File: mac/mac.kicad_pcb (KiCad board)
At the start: 2 copper layers, 5 parts

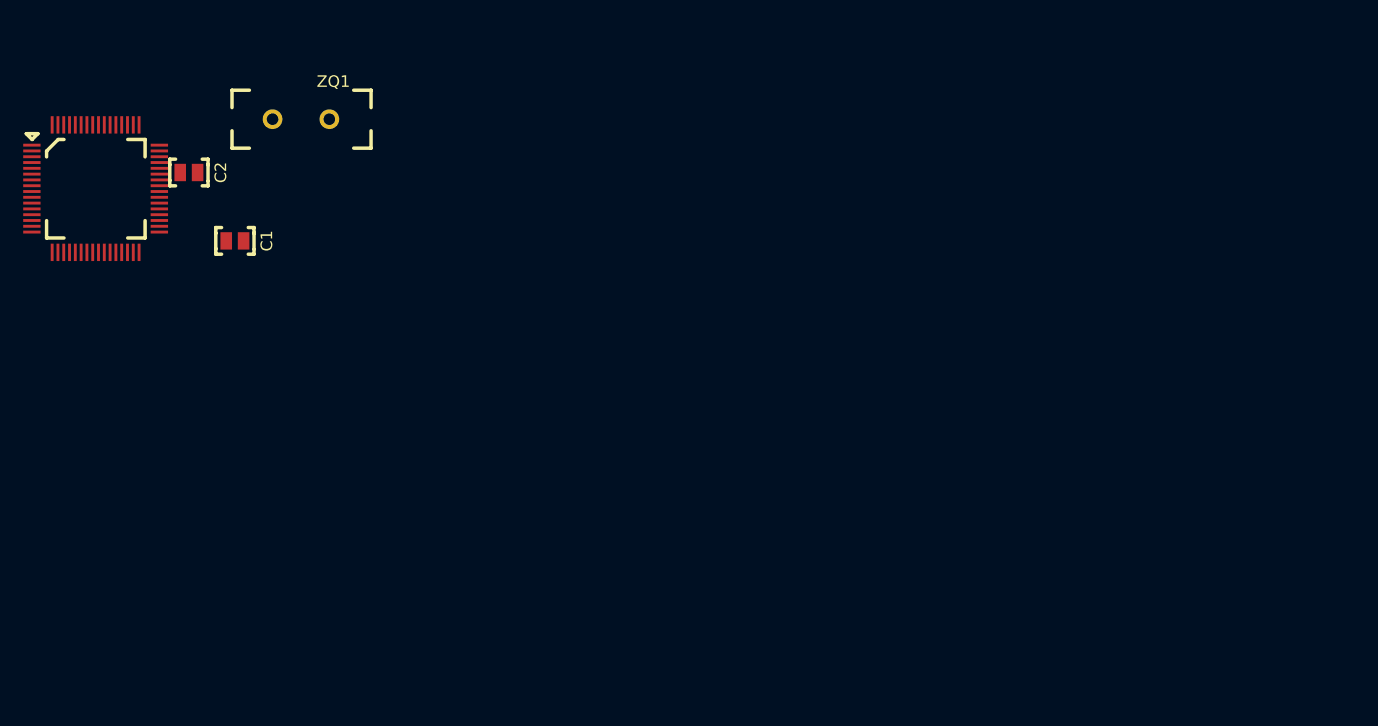
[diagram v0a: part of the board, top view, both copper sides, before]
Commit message: на схеме (-), на трассировке (*)
-поставлен uart-rs485
-поставлена микросхема CAN
-CAN и RS выведены наружу
-выводные разъемы
*определен максимальный габарит 45х70
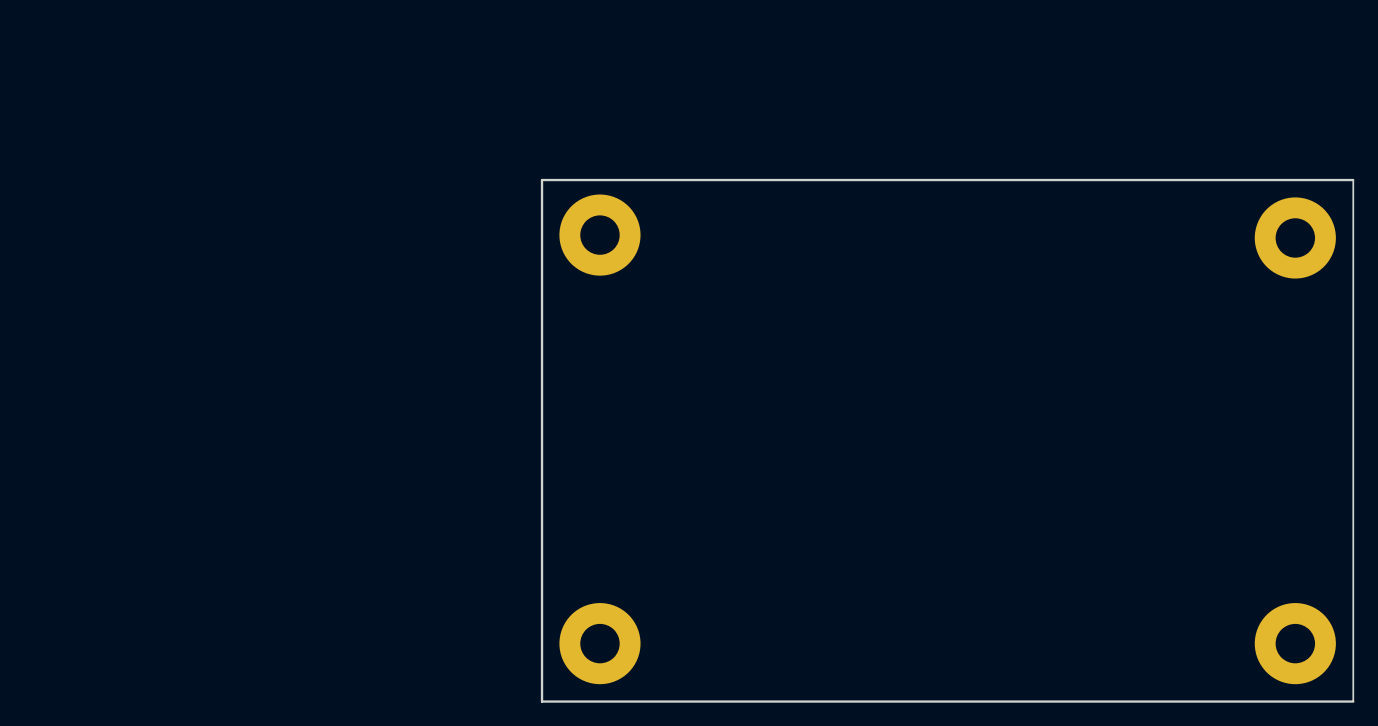
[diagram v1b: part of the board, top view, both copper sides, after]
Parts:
- removed C1, C2: 12пФ, N_RLC:Конденсатор_SMD_0603
- removed DD1: 1986ВЕ92QL, N_DD:Микросхема_1986ВЕ92QL
- removed ZQ1: 16М, N_RLC:Резонатор_РК456МДУ(DIP)
- added M3: Отверстие_М3, N_X:Отверстие_М3, F.Cu at (160.0, 112.5)
- added M3: Отверстие_М3, N_X:Отверстие_М3, F.Cu at (220.0, 112.5)
- added M3: Отверстие_М3, N_X:Отверстие_М3, F.Cu at (220.0, 77.5)
- added M3: Отверстие_М3, N_X:Отверстие_М3, F.Cu at (160.0, 77.2)
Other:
- board outline added: 70 x 45 mm

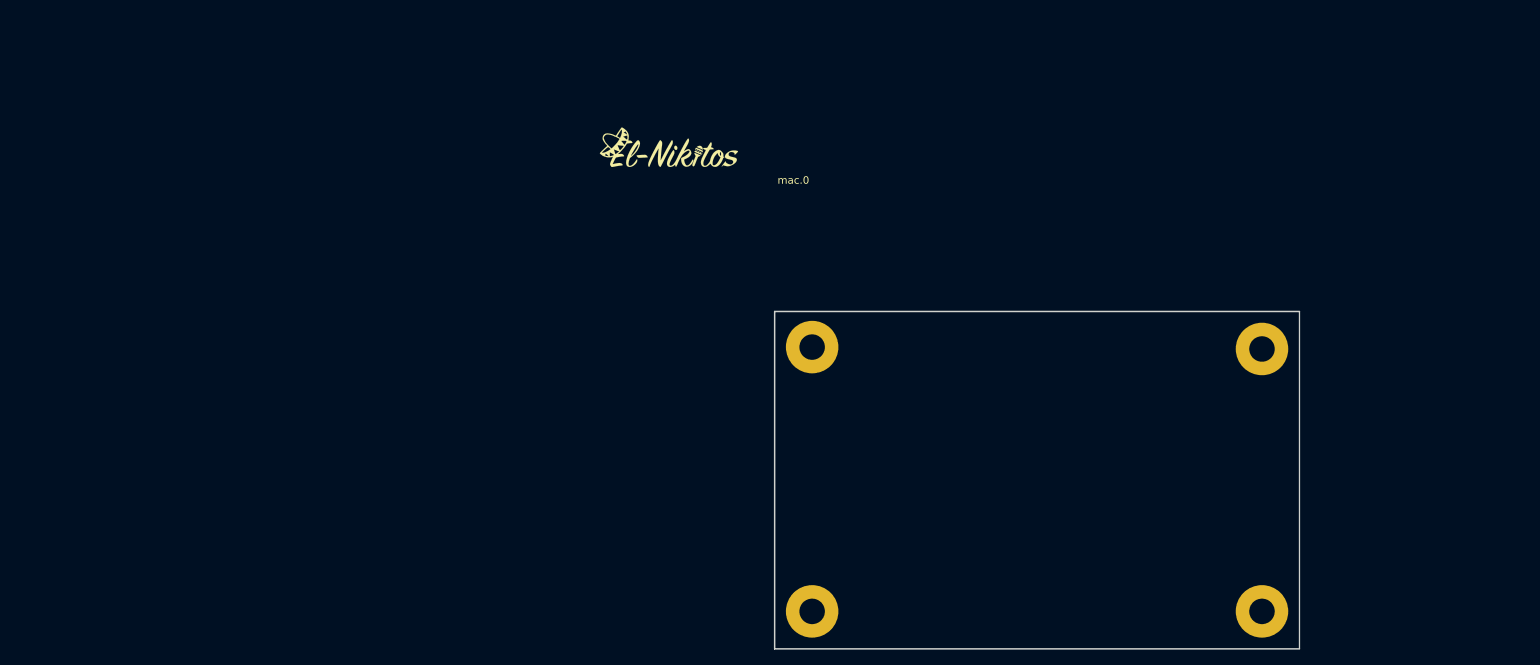
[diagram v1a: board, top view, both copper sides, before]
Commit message: трассировка в самом разгаре
выведены GPIO
не выведены ответвления на RS и CAN
не выведено программирование
не разведена земля
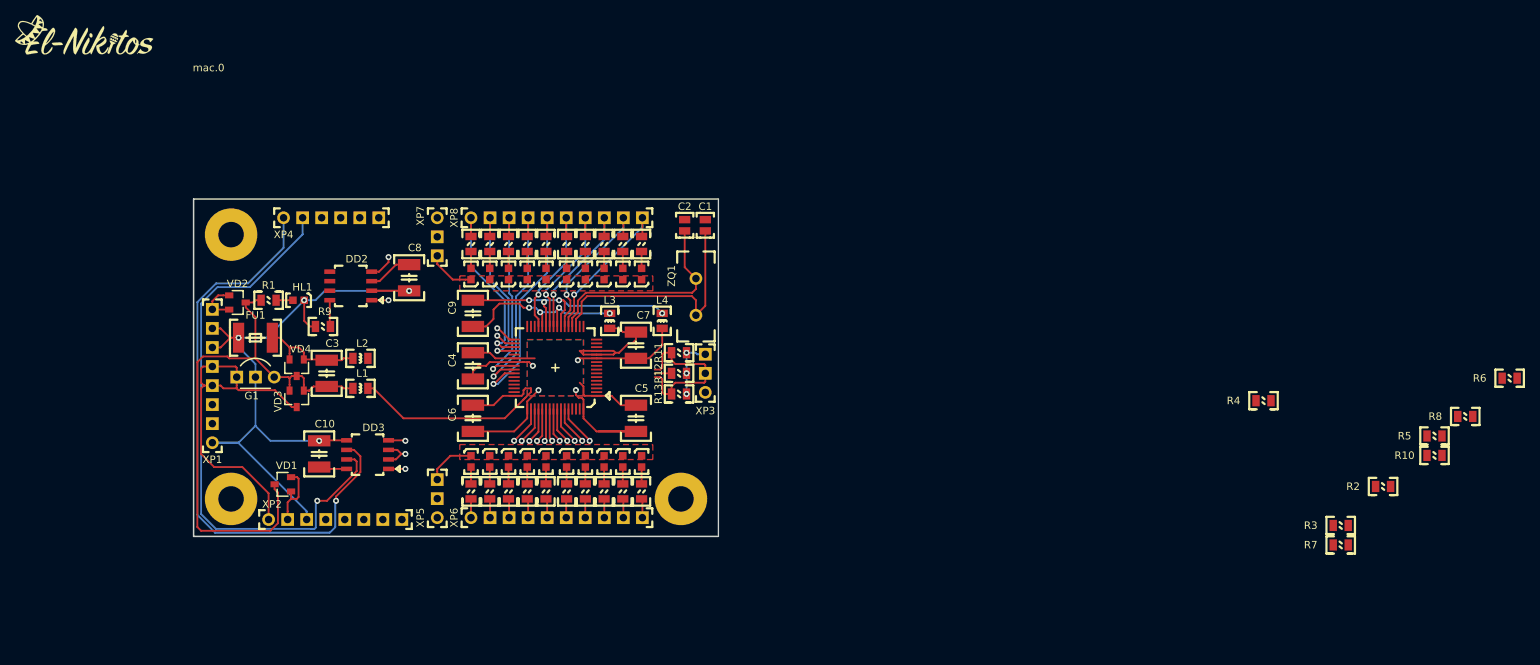
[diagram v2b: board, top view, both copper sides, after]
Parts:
- removed the M3 at (160.0, 112.5)
- removed the M3 at (220.0, 112.5)
- removed the M3 at (220.0, 77.5)
- added C1: 12пФ(0603), N_RLC:Конденсатор_SMD_0603, F.Cu at (145.8, 61.8)
- added C10: 4,7мкФ(1210), N_RLC:Конденсатор_SMD_1210, F.Cu at (94.2, 89.8)
- added C2: 12пФ(0603), N_RLC:Конденсатор_SMD_0603, F.Cu at (143.0, 61.8)
- added C3: 4,7мкФ(1210), N_RLC:Конденсатор_SMD_1210, F.Cu at (95.2, 82.5)
- added C4: 4,7мкФ(1210), N_RLC:Конденсатор_SMD_1210, F.Cu at (114.8, 78.0)
- added C5: 4,7мкФ(1210), N_RLC:Конденсатор_SMD_1210, F.Cu at (136.5, 85.0)
- added C6: 4,7мкФ(1210), N_RLC:Конденсатор_SMD_1210, F.Cu at (114.8, 85.0)
- added C7: 4,7мкФ(1210), N_RLC:Конденсатор_SMD_1210, F.Cu at (136.5, 75.2)
- added C8: 4,7мкФ(1210), N_RLC:Конденсатор_SMD_1210, F.Cu at (106.2, 69.8)
- added C9: 4,7мкФ(1210), N_RLC:Конденсатор_SMD_1210, F.Cu at (114.8, 74.5)
- added DD1: 1986ВЕ92QL, N_DD:Микросхема_1986ВЕ92QL, F.Cu at (137.0, 87.7)
- added DD2: 5559ИН14А(CAN), N_DD:SO-8, F.Cu at (98.5, 69.1)
- added DD3: 5559ИН10_28(UART-RS485), N_DD:SO-8, F.Cu at (100.7, 91.6)
- added FU1: Предохранитель, N_RLC:Предохранитель_SMD_1812, F.Cu at (83.5, 76.0)
- added G1: стабилизатор_нерегулируемый_LM2950, N_G:Стабилизатор_корпус_TO-92, F.Cu at (88.2, 81.2)
- added HL1: Светодиод, N_VD_HL:Светодиод_SMD_0603, F.Cu at (90.8, 71.0)
- added HL10: Светодиод, N_VD_HL:Светодиод_SMD_0603, F.Cu at (134.8, 93.2)
- added HL11: Светодиод, N_VD_HL:Светодиод_SMD_0603, F.Cu at (137.2, 93.2)
- added HL12: Светодиод, N_VD_HL:Светодиод_SMD_0603, F.Cu at (114.5, 66.8)
- added HL13: Светодиод, N_VD_HL:Светодиод_SMD_0603, F.Cu at (117.0, 66.8)
- added HL14: Светодиод, N_VD_HL:Светодиод_SMD_0603, F.Cu at (119.5, 66.8)
- added HL15: Светодиод, N_VD_HL:Светодиод_SMD_0603, F.Cu at (122.0, 66.8)
- added HL16: Светодиод, N_VD_HL:Светодиод_SMD_0603, F.Cu at (124.5, 66.8)
- added HL17: Светодиод, N_VD_HL:Светодиод_SMD_0603, F.Cu at (127.2, 66.8)
- added HL18: Светодиод, N_VD_HL:Светодиод_SMD_0603, F.Cu at (129.8, 66.8)
- added HL19: Светодиод, N_VD_HL:Светодиод_SMD_0603, F.Cu at (132.2, 66.8)
- added HL2: Светодиод, N_VD_HL:Светодиод_SMD_0603, F.Cu at (114.5, 93.2)
- added HL20: Светодиод, N_VD_HL:Светодиод_SMD_0603, F.Cu at (134.8, 66.8)
- added HL21: Светодиод, N_VD_HL:Светодиод_SMD_0603, F.Cu at (137.2, 66.8)
- added HL3: Светодиод, N_VD_HL:Светодиод_SMD_0603, F.Cu at (117.0, 93.2)
- added HL4: Светодиод, N_VD_HL:Светодиод_SMD_0603, F.Cu at (119.5, 93.2)
- added HL5: Светодиод, N_VD_HL:Светодиод_SMD_0603, F.Cu at (122.0, 93.2)
- added HL6: Светодиод, N_VD_HL:Светодиод_SMD_0603, F.Cu at (124.5, 93.2)
- added HL7: Светодиод, N_VD_HL:Светодиод_SMD_0603, F.Cu at (127.2, 93.2)
- added HL8: Светодиод, N_VD_HL:Светодиод_SMD_0603, F.Cu at (129.8, 93.2)
- added HL9: Светодиод, N_VD_HL:Светодиод_SMD_0603, F.Cu at (132.2, 93.2)
- added L1: 33мкГн(0805), N_RLC:Чип-индуктивность_SMD_0805, F.Cu at (98.8, 82.8)
- added L2: 33мкГн(0805), N_RLC:Чип-индуктивность_SMD_0805, F.Cu at (98.8, 78.8)
- added L3: 33мкГн(0805), N_RLC:Чип-индуктивность_SMD_0805, F.Cu at (133.0, 74.8)
- added L4: 33мкГн(0805), N_RLC:Чип-индуктивность_SMD_0805, F.Cu at (140.0, 74.8)
- added M3: Отверстие_М3, N_X:Отверстие_М3, F.Cu at (82.5, 97.5)
- added M3: Отверстие_М3, N_X:Отверстие_М3, F.Cu at (142.5, 97.5)
- added R1: 39, N_RLC:Резистор_SMD_0805_0,125Вт, F.Cu at (88.5, 71.0)
- added R10: 20к, N_RLC:Резистор_SMD_0805_0,125Вт, F.Cu at (242.0, 91.7)
- added R11: 20к, N_RLC:Резистор_SMD_0805_0,125Вт, F.Cu at (141.2, 78.0)
- added R12: 20к, N_RLC:Резистор_SMD_0805_0,125Вт, F.Cu at (141.2, 80.8)
- added R13: 20к, N_RLC:Резистор_SMD_0805_0,125Вт, F.Cu at (141.2, 83.5)
- added R14: 39, N_RLC:Резистор_SMD_0805_0,125Вт, F.Cu at (114.5, 95.5)
- added R15: 39, N_RLC:Резистор_SMD_0805_0,125Вт, F.Cu at (117.0, 95.5)
- added R16: 39, N_RLC:Резистор_SMD_0805_0,125Вт, F.Cu at (119.5, 95.5)
- added R17: 39, N_RLC:Резистор_SMD_0805_0,125Вт, F.Cu at (122.0, 95.5)
- added R18: 39, N_RLC:Резистор_SMD_0805_0,125Вт, F.Cu at (124.5, 95.5)
- added R19: 39, N_RLC:Резистор_SMD_0805_0,125Вт, F.Cu at (127.2, 95.5)
- added R2: 20к, N_RLC:Резистор_SMD_0805_0,125Вт, F.Cu at (235.2, 95.8)
- added R20: 39, N_RLC:Резистор_SMD_0805_0,125Вт, F.Cu at (129.8, 95.5)
- added R21: 39, N_RLC:Резистор_SMD_0805_0,125Вт, F.Cu at (132.2, 95.5)
- added R22: 39, N_RLC:Резистор_SMD_0805_0,125Вт, F.Cu at (134.8, 95.5)
- added R23: 39, N_RLC:Резистор_SMD_0805_0,125Вт, F.Cu at (137.2, 95.5)
- added R24: 39, N_RLC:Резистор_SMD_0805_0,125Вт, F.Cu at (114.5, 64.5)
- added R25: 39, N_RLC:Резистор_SMD_0805_0,125Вт, F.Cu at (117.0, 64.5)
- added R26: 39, N_RLC:Резистор_SMD_0805_0,125Вт, F.Cu at (119.5, 64.5)
- added R27: 39, N_RLC:Резистор_SMD_0805_0,125Вт, F.Cu at (122.0, 64.5)
- added R28: 39, N_RLC:Резистор_SMD_0805_0,125Вт, F.Cu at (124.5, 64.5)
- added R29: 39, N_RLC:Резистор_SMD_0805_0,125Вт, F.Cu at (127.2, 64.5)
- added R3: 20к, N_RLC:Резистор_SMD_0805_0,125Вт, F.Cu at (229.5, 101.0)
- added R30: 39, N_RLC:Резистор_SMD_0805_0,125Вт, F.Cu at (129.8, 64.5)
- added R31: 39, N_RLC:Резистор_SMD_0805_0,125Вт, F.Cu at (132.2, 64.5)
- added R32: 39, N_RLC:Резистор_SMD_0805_0,125Вт, F.Cu at (134.8, 64.5)
- added R33: 39, N_RLC:Резистор_SMD_0805_0,125Вт, F.Cu at (137.2, 64.5)
- added R4: 20к, N_RLC:Резистор_SMD_0805_0,125Вт, F.Cu at (219.2, 84.4)
- added R5: 20к, N_RLC:Резистор_SMD_0805_0,125Вт, F.Cu at (242.0, 89.1)
- added R6: 20к, N_RLC:Резистор_SMD_0805_0,125Вт, F.Cu at (252.0, 81.4)
- added R7: 20к, N_RLC:Резистор_SMD_0805_0,125Вт, F.Cu at (229.5, 103.6)
- added R8: 100к, N_RLC:Резистор_SMD_0805_0,125Вт, F.Cu at (246.1, 86.5)
- added R9: 24к, N_RLC:Резистор_SMD_0805_0,125Вт, F.Cu at (93.8, 74.5)
- added VD1: BAR43CFILM, N_VD_HL:Диод_BAR43CFILM_SOT-23, F.Cu at (89.4, 95.5)
- added VD2: BAR43CFILM, N_VD_HL:Диод_BAR43CFILM_SOT-23, F.Cu at (83.3, 71.3)
- added VD3: BAR43CFILM, N_VD_HL:Диод_BAR43CFILM_SOT-23, F.Cu at (91.2, 84.2)
- added VD4: BAR43CFILM, N_VD_HL:Диод_BAR43CFILM_SOT-23, F.Cu at (91.2, 80.0)
- added XP1: Вилка_PLS8, N_X:Вилка_PLS8_вертикальная, F.Cu at (80.0, 90.0)
- added XP2: Вилка_PLS8, N_X:Вилка_PLS8_вертикальная, F.Cu at (87.5, 100.2)
- added XP3: Вилка_PLS3, N_X:Вилка_PLS3_вертикальная, F.Cu at (145.8, 83.3)
- added XP4: Вилка_PLS6, N_X:Вилка_PLS6_вертикальная, F.Cu at (89.5, 60.0)
- added XP5: Вилка_PLS3, N_X:Вилка_PLS3_вертикальная, F.Cu at (110.0, 100.0)
- added XP6: Вилка_PLS10, N_X:Вилка_PLS10_вертикальная, F.Cu at (114.5, 100.0)
- added XP7: Вилка_PLS3, N_X:Вилка_PLS3_вертикальная, F.Cu at (110.0, 60.0)
- added XP8: Вилка_PLS10, N_X:Вилка_PLS10_вертикальная, F.Cu at (114.5, 60.0)
- added ZQ1: 16М, N_RLC:Резонатор_РК456МДУ(DIP), F.Cu at (144.5, 73.0)
- moved G*** 79.4 mm to (63.2, 36.0)
- moved M3 78.9 mm to (82.5, 62.2)
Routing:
- net /GND: track 0.00 -> 91.6 mm, vias 0 -> 4
- net /VCC: track 0.00 -> 84.7 mm
- net /RS_A: track 0.00 -> 79.6 mm, vias 0 -> 1
- net /RS_B: track 0.00 -> 77.4 mm, vias 0 -> 1
- net /VCC_MC: track 0.00 -> 70.1 mm
- net /GND_MC: track 0.00 -> 61.4 mm, vias 0 -> 7
- net /+4...30: track 0.00 -> 47.6 mm
- net /A_GND_MC: track 0.00 -> 35.1 mm, vias 0 -> 4
- net Net-(C1-Pad1): track 0.00 -> 33.2 mm
- net /PC0_SCL1: track 0.00 -> 31.4 mm, vias 0 -> 1
- net /PC1_SDA1: track 0.00 -> 28.7 mm, vias 0 -> 1
- net Net-(C2-Pad1): track 0.00 -> 28.5 mm
- net /PC2: track 0.00 -> 26.9 mm, vias 0 -> 1
- net /A_VCC_MC: track 0.00 -> 25.9 mm, vias 0 -> 4
- net /PD6_ADC6: track 0.00 -> 24.4 mm, vias 0 -> 1
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- added copper zone on F.Cu, net /GND_LED1
- added copper zone on F.Cu, net /GND_LED2
- added copper zone on B.Cu, net /GND_MC
- added copper zone on F.Cu, net /VCC_MC

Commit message: закончена разводка, не проводилась стилистическая проверка
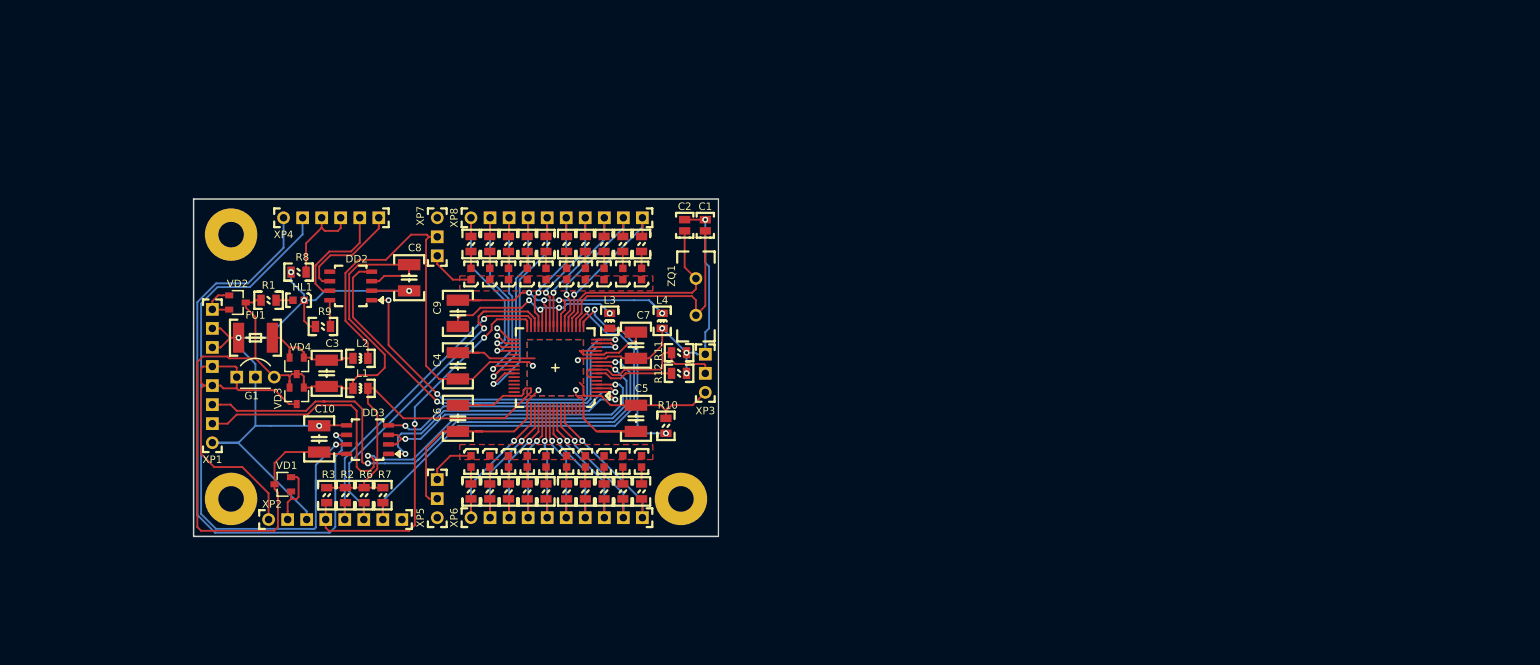
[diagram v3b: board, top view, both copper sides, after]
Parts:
- removed the G*** at (63.2, 36.0)
- removed R13, R4, R5: 20к, N_RLC:Резистор_SMD_0805_0,125Вт
- added G***: LOGO, N_ICO:el-nikitos_43x15, B.Cu at (117.2, 68.5)
- moved R8 156.8 mm to (90.5, 67.2)
- moved R6 152.5 mm to (100.2, 96.0), turned to 270 degrees
- moved R2 137.4 mm to (97.8, 96.0), turned to 270 degrees
- moved R3 134.3 mm to (95.2, 96.0), turned to 270 degrees
- moved R7 127.0 mm to (102.8, 96.0), turned to 270 degrees
- moved R10 101.6 mm to (140.5, 86.8), turned to 270 degrees
- moved C10 2.00 mm to (94.2, 87.8)
- moved C4 2.00 mm to (112.8, 78.0)
- moved C6 2.00 mm to (112.8, 85.0)
- moved C9 2.00 mm to (112.8, 74.5)
- moved DD3 2.00 mm to (100.7, 89.6)
- moved VD3 0.40 mm to (91.2, 83.8)
- moved VD4 0.25 mm to (91.2, 79.8)
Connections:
- net /TCK_TX renamed /TCK_CLK_TX
- net /TMS_RX renamed /TMS_DIO_RX
- DD1 pad 30: /TDO -> /TDO_SWO
- DD1 pad 33: /TRST -> Net-(DD1-Pad33)
- DD1 pad 34: /TDI -> Net-(DD1-Pad34)
- R6 pad 2: /TDO -> /TDO_SWO
- XP2 pad 6: /TRST -> /TDO_SWO
- XP2 pad 7: /TDI -> /RES
- XP2 pad 8: /TDO -> Net-(XP2-Pad8)
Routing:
- net /GND_MC: track 61.4 -> 151.8 mm, vias 7 -> 8
- net /USB_D+: track 0.00 -> 78.7 mm, vias 0 -> 2
- net /USB_D-: track 0.00 -> 77.4 mm, vias 0 -> 2
- net /RES: track 0.00 -> 62.9 mm, vias 0 -> 1
- net /PE6_C2-TX: track 3.45 -> 57.2 mm, vias 1 -> 2
- net /TCK_CLK_TX: track 0.00 -> 52.6 mm, vias 0 -> 2
- net /PE6_C2-RX: track 2.25 -> 51.0 mm, vias 1 -> 3
- net /TDO_SWO: track 0.00 -> 47.2 mm, vias 0 -> 1
- net /TMS_DIO_RX: track 0.00 -> 44.3 mm, vias 0 -> 1
- net /VCC: track 84.7 -> 126.5 mm
- net /VCC_MC: track 70.1 -> 106.9 mm
- net /PF2_U2-En: track 4.49 -> 41.2 mm, vias 1 -> 2
- net /PF0_U2-RX: track 2.25 -> 38.9 mm, vias 1 -> 2
- net /PF1_U2-TX: track 2.27 -> 35.2 mm, vias 1 -> 2
- net Net-(DD1-Pad17): track 0.00 -> 25.8 mm, vias 0 -> 2
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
